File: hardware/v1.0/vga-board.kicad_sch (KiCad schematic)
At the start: 15 parts, among them J10 Conn_01x06, J9 Conn_01x34, U6 74LVC245A, U7 TLV62568DRL

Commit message: finished first draft, still DRC errors
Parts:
- D2: footprint LED_SMD:LED_0402_1005Metric_Pad0.77x0.64mm_HandSolder -> LED_SMD:LED_0805_2012Metric
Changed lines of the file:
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@@
 			)
 		)
-		(property "Footprint" "LED_SMD:LED_0402_1005Metric_Pad0.77x0.64mm_HandSolder"
+		(property "Footprint" "LED_SMD:LED_0805_2012Metric"
 			(at 184.15 64.77 90)
 			(effects

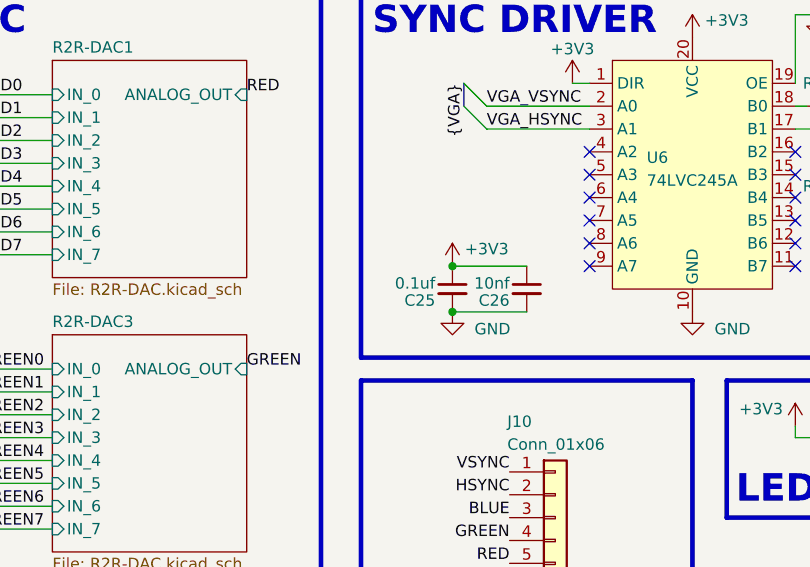
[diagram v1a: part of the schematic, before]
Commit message: added tvs diode+changed inductors
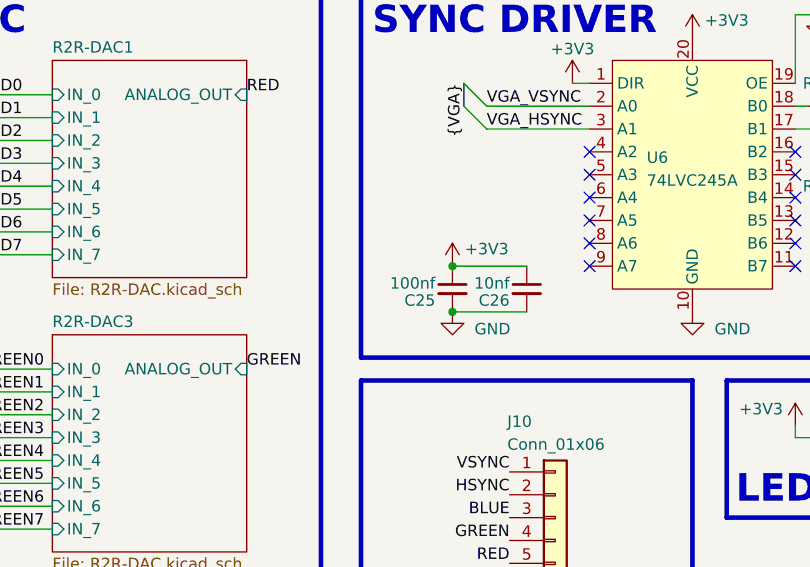
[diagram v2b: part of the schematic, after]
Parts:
- C25: value 0.1uf -> 100nf
- L2: footprint Inductor_SMD:L_0603_1608Metric -> Inductor_SMD:L_0805_2012Metric
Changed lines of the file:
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@@
 			)
 		)
-		(property "Value" "0.1uf"
+		(property "Value" "100nf"
 			(at 131.445 47.625 0)
 			(effects
@@
 			)
 		)
-		(property "Footprint" "Inductor_SMD:L_0603_1608Metric"
+		(property "Footprint" "Inductor_SMD:L_0805_2012Metric"
 			(at 228.6 26.67 0)
 			(effects
